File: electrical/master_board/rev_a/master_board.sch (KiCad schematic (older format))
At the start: 4 parts

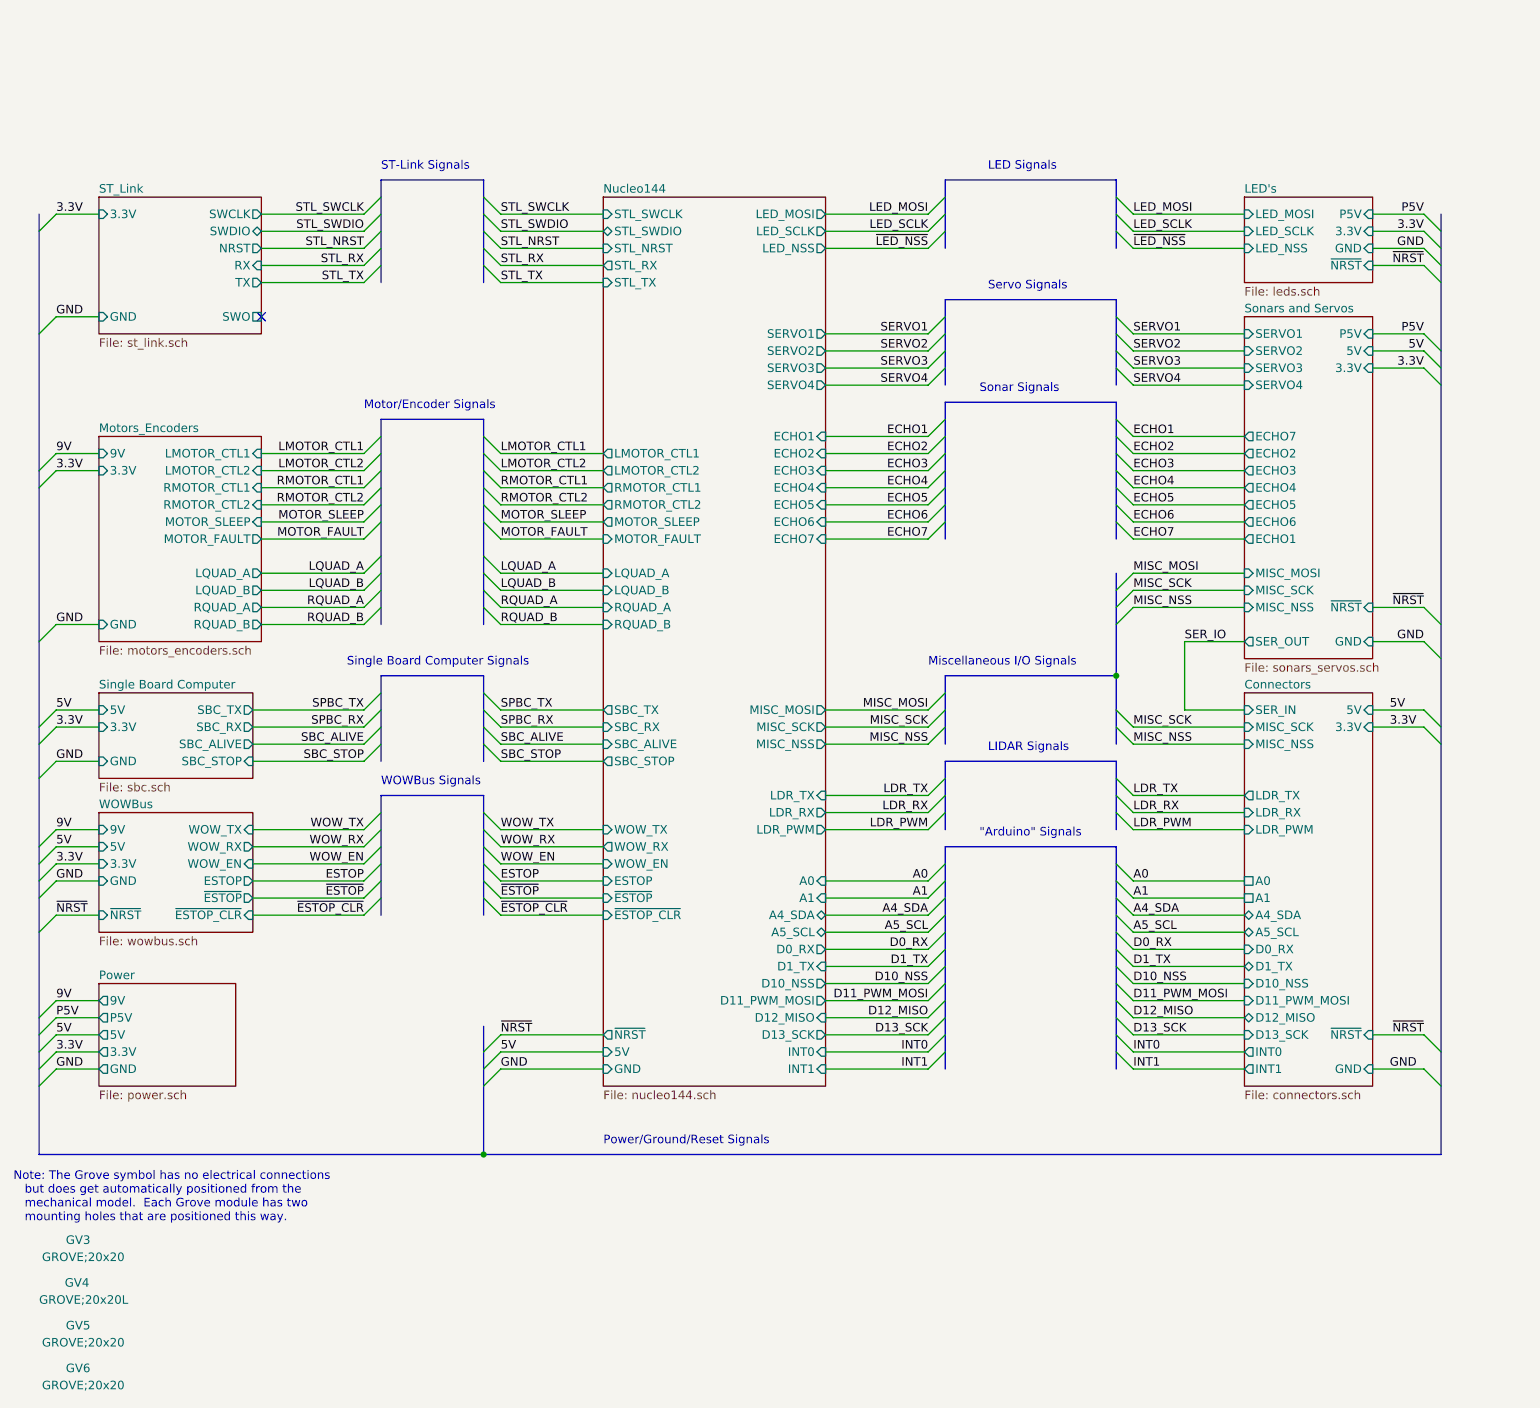
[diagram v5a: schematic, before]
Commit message: Bound signals to Morpho pins.
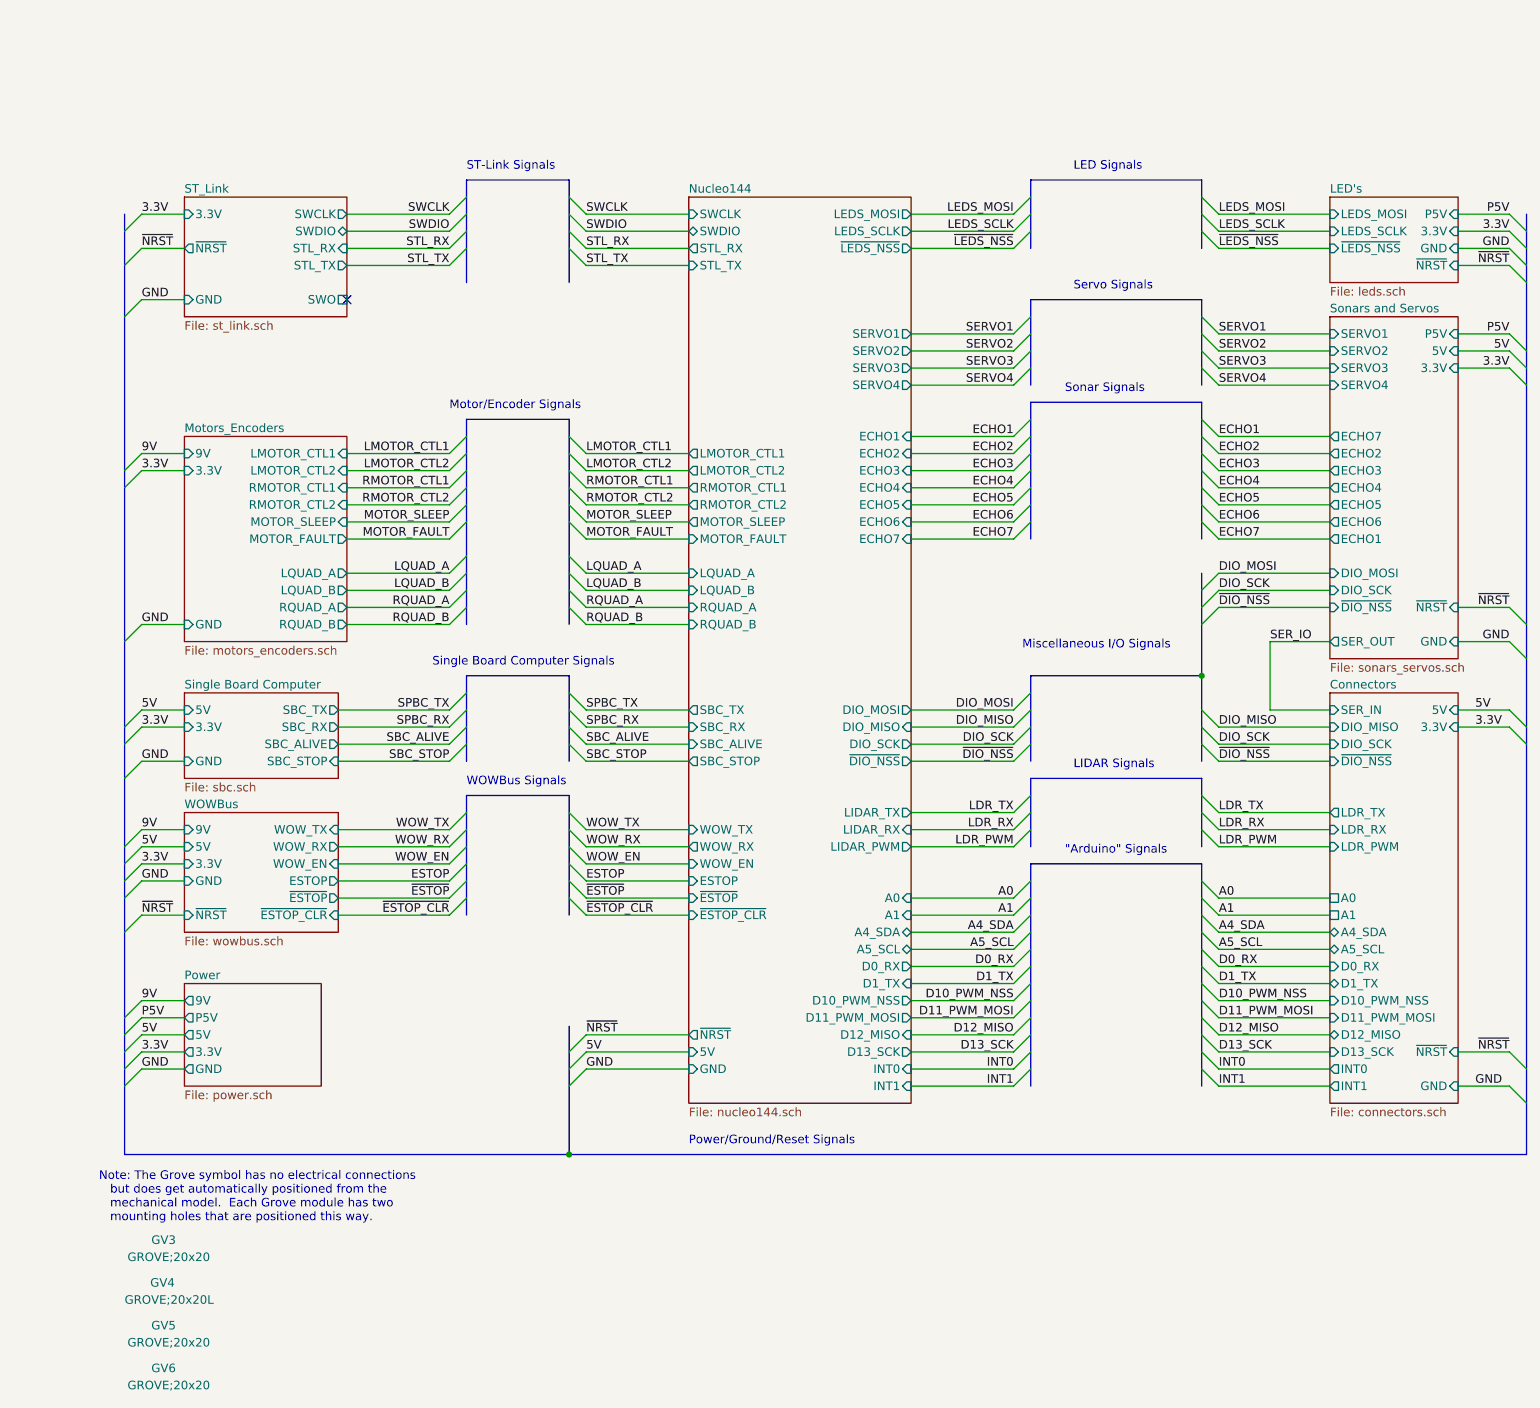
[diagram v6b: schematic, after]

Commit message: Schematic is basically complete.
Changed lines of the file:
@@
 RMOTOR_CTL1
 Text Label 4000 2800 0    50   ~ 0
-MOTOR_SLEEP
+~MOTOR_SLEEP
 Text Label 4000 2900 0    50   ~ 0
-MOTOR_FAULT
+~MOTOR_FAULT
 Text Label 4000 3100 0    50   ~ 0
 LQUAD_A
@@
 LQUAD_A
 Text Label 3200 2900 2    50   ~ 0
-MOTOR_FAULT
-Text Label 3200 2800 2    50   ~ 0
-MOTOR_SLEEP
+~MOTOR_FAULT
 Text Label 3200 2600 2    50   ~ 0
 RMOTOR_CTL1
@@
 Wire Bus Line
 	3900 2200 3300 2200
-$Sheet
-S 1650 2300 950  1200
-U 5F4A826A
-F0 "Motors_Encoders" 50
-F1 "motors_encoders.sch" 50
-F2 "LMOTOR_CTL2" I R 2600 2500 50
-F3 "RMOTOR_CTL2" I R 2600 2700 50
-F4 "RMOTOR_CTL1" I R 2600 2600 50
-F5 "9V" I L 1650 2400 50
-F6 "LMOTOR_CTL1" I R 2600 2400 50
-F7 "MOTOR_SLEEP" I R 2600 2800 50
-F8 "MOTOR_FAULT" O R 2600 2900 50
-F9 "3.3V" I L 1650 2500 50
-F10 "LQUAD_B" O R 2600 3200 50
-F11 "LQUAD_A" O R 2600 3100 50
-F12 "RQUAD_A" O R 2600 3300 50
-F13 "RQUAD_B" O R 2600 3400 50
-F14 "GND" I L 1650 3400 50
-$EndSheet
 Text Label 7700 5700 0    50   ~ 0
 D11_PWM_MOSI
@@
 ~NRST
 $Sheet
-S 1650 4500 900  700
+S 1650 4500 900  800
 U 5F8C2F57
 F0 "WOWBus" 50
@@
 F2 "9V" I L 1650 4600 50
 F3 "GND" I L 1650 4900 50
-F4 "WOW_EN" I R 2550 4800 50
-F5 "3.3V" I L 1650 4800 50
-F6 "5V" I L 1650 4700 50
-F7 "WOW_TX" I R 2550 4600 50
-F8 "WOW_RX" O R 2550 4700 50
-F9 "ESTOP" O R 2550 4900 50
-F10 "~ESTOP" O R 2550 5000 50
-F11 "~ESTOP_CLR" I R 2550 5100 50
-F12 "~NRST" I L 1650 5100 50
+F4 "3.3V" I L 1650 4800 50
+F5 "5V" I L 1650 4700 50
+F6 "WOW_TX" I R 2550 4600 50
+F7 "WOW_RX" O R 2550 4700 50
+F8 "~ESTOP_CLR" I R 2550 5100 50
+F9 "~NRST" I L 1650 5100 50
+F10 "~MOTOR_FAULT" I R 2550 5200 50
+F11 "ESTOP" O R 2550 4900 50
+F12 "~ESTOP" O R 2550 5000 50
+F13 "WOW_EN" I R 2550 4800 50
 $EndSheet
 Wire Wire Line
@@
 F6 "3.3V" I L 1650 4000 50
 F7 "SBC_ALIVE" O R 2550 4100 50
-F8 "SBC_STOP" I R 2550 4200 50
 $EndSheet
-Text Label 3200 4200 2    50   ~ 0
-SBC_STOP
 Wire Wire Line
 	2550 3900 3200 3900
@@
 Wire Wire Line
 	2550 4100 3200 4100
-Wire Wire Line
-	2550 4200 3200 4200
-Entry Wire Line
-	3300 4100 3200 4200
 Entry Wire Line
 	3300 4000 3200 4100
@@
 Entry Wire Line
 	3200 3900 3300 3800
-Entry Wire Line
-	3900 4100 4000 4200
 Entry Wire Line
 	3900 4000 4000 4100
@@
 Text Label 4000 4100 0    50   ~ 0
 SBC_ALIVE
-Text Label 4000 4200 0    50   ~ 0
-SBC_STOP
 Wire Wire Line
 	4000 3900 4600 3900
@@
 Wire Wire Line
 	4000 4100 4600 4100
-Wire Wire Line
-	4000 4200 4600 4200
 Wire Bus Line
 	3300 3700 3900 3700
@@
 Text Notes 6800 4750 0    50   ~ 0
 "Arduino" Signals
-$Sheet
-S 4600 900  1300 5300
-U 5F3221A2
-F0 "Nucleo144" 50
-F1 "nucleo144.sch" 50
-F2 "GND" I L 4600 6000 50
-F3 "5V" I L 4600 5900 50
-F4 "STL_RX" O L 4600 1200 50
-F5 "STL_TX" I L 4600 1300 50
-F6 "LMOTOR_CTL1" O L 4600 2400 50
-F7 "LMOTOR_CTL2" O L 4600 2500 50
-F8 "RMOTOR_CTL1" O L 4600 2600 50
-F9 "RMOTOR_CTL2" O L 4600 2700 50
-F10 "MOTOR_SLEEP" O L 4600 2800 50
-F11 "MOTOR_FAULT" I L 4600 2900 50
-F12 "LQUAD_A" I L 4600 3100 50
-F13 "LQUAD_B" I L 4600 3200 50
-F14 "RQUAD_A" I L 4600 3300 50
-F15 "RQUAD_B" I L 4600 3400 50
-F16 "ECHO1" I R 5900 2300 50
-F17 "ECHO2" I R 5900 2400 50
-F18 "ECHO3" I R 5900 2500 50
-F19 "ECHO4" I R 5900 2600 50
-F20 "ECHO5" I R 5900 2700 50
-F21 "ECHO6" I R 5900 2800 50
-F22 "ECHO7" I R 5900 2900 50
-F23 "SERVO2" O R 5900 1800 50
-F24 "SERVO1" O R 5900 1700 50
-F25 "SERVO3" O R 5900 1900 50
-F26 "SERVO4" O R 5900 2000 50
-F27 "A0" I R 5900 5000 50
-F28 "A1" I R 5900 5100 50
-F29 "A4_SDA" B R 5900 5200 50
-F30 "A5_SCL" B R 5900 5300 50
-F31 "D0_RX" O R 5900 5400 50
-F32 "D1_TX" I R 5900 5500 50
-F33 "D11_PWM_MOSI" O R 5900 5700 50
-F34 "D12_MISO" I R 5900 5800 50
-F35 "D13_SCK" O R 5900 5900 50
-F36 "~NRST" O L 4600 5800 50
-F37 "INT0" I R 5900 6000 50
-F38 "INT1" I R 5900 6100 50
-F39 "WOW_TX" I L 4600 4600 50
-F40 "WOW_RX" O L 4600 4700 50
-F41 "WOW_EN" I L 4600 4800 50
-F42 "ESTOP" I L 4600 4900 50
-F43 "~ESTOP" I L 4600 5000 50
-F44 "~ESTOP_CLR" I L 4600 5100 50
-F45 "SBC_TX" O L 4600 3900 50
-F46 "SBC_RX" I L 4600 4000 50
-F47 "SBC_ALIVE" I L 4600 4100 50
-F48 "SBC_STOP" O L 4600 4200 50
-F49 "LEDS_MOSI" O R 5900 1000 50
-F50 "LEDS_SCLK" O R 5900 1100 50
-F51 "SWCLK" I L 4600 1000 50
-F52 "SWDIO" B L 4600 1100 50
-F53 "D10_PWM_NSS" O R 5900 5600 50
-F54 "LIDAR_PWM" O R 5900 4700 50
-F55 "LIDAR_TX" O R 5900 4500 50
-F56 "LIDAR_RX" I R 5900 4600 50
-F57 "DIO_MOSI" O R 5900 3900 50
-F58 "DIO_SCK" O R 5900 4100 50
-F59 "DIO_MISO" I R 5900 4000 50
-F60 "~DIO_NSS" O R 5900 4200 50
-F61 "~LEDS_NSS" O R 5900 1200 50
-$EndSheet
 Entry Wire Line
 	6500 3900 6600 3800
@@
 Text Label 1400 1200 0    50   ~ 0
 ~NRST
+$Sheet
+S 1650 2300 950  1200
+U 5F4A826A
+F0 "Motors_Encoders" 50
+F1 "motors_encoders.sch" 50
+F2 "LMOTOR_CTL2" I R 2600 2500 50
+F3 "RMOTOR_CTL2" I R 2600 2700 50
+F4 "RMOTOR_CTL1" I R 2600 2600 50
+F5 "9V" I L 1650 2400 50
+F6 "LMOTOR_CTL1" I R 2600 2400 50
+F7 "3.3V" I L 1650 2500 50
+F8 "LQUAD_B" O R 2600 3200 50
+F9 "LQUAD_A" O R 2600 3100 50
+F10 "RQUAD_A" O R 2600 3300 50
+F11 "RQUAD_B" O R 2600 3400 50
+F12 "GND" I L 1650 3400 50
+F13 "~MOTOR_SLEEP" I R 2600 2800 50
+F14 "~MOTOR_FAULT" O R 2600 2900 50
+$EndSheet
+Text Label 3200 2800 2    50   ~ 0
+~MOTOR_SLEEP
+Entry Wire Line
+	3200 5200 3300 5100
+Entry Wire Line
+	4000 5200 3900 5100
+Wire Wire Line
+	2550 5200 3200 5200
+Wire Wire Line
+	4600 5200 4000 5200
+Text Label 3200 5200 2    50   ~ 0
+~MOTOR_FAULT
+Text Label 4000 5200 0    50   ~ 0
+~MOTOR_FAULT
+$Sheet
+S 4600 900  1300 5300
+U 5F3221A2
+F0 "Nucleo144" 50
+F1 "nucleo144.sch" 50
+F2 "GND" I L 4600 6000 50
+F3 "5V" I L 4600 5900 50
+F4 "STL_RX" O L 4600 1200 50
+F5 "STL_TX" I L 4600 1300 50
+F6 "LMOTOR_CTL1" O L 4600 2400 50
+F7 "LMOTOR_CTL2" O L 4600 2500 50
+F8 "RMOTOR_CTL1" O L 4600 2600 50
+F9 "RMOTOR_CTL2" O L 4600 2700 50
+F10 "LQUAD_A" I L 4600 3100 50
+F11 "LQUAD_B" I L 4600 3200 50
+F12 "RQUAD_A" I L 4600 3300 50
+F13 "RQUAD_B" I L 4600 3400 50
+F14 "ECHO1" I R 5900 2300 50
+F15 "ECHO2" I R 5900 2400 50
+F16 "ECHO3" I R 5900 2500 50
+F17 "ECHO4" I R 5900 2600 50
+F18 "ECHO5" I R 5900 2700 50
+F19 "ECHO6" I R 5900 2800 50
+F20 "ECHO7" I R 5900 2900 50
+F21 "SERVO2" O R 5900 1800 50
+F22 "SERVO1" O R 5900 1700 50
+F23 "SERVO3" O R 5900 1900 50
+F24 "SERVO4" O R 5900 2000 50
+F25 "A0" I R 5900 5000 50
+F26 "A1" I R 5900 5100 50
+F27 "A4_SDA" B R 5900 5200 50
+F28 "A5_SCL" B R 5900 5300 50
+F29 "D0_RX" O R 5900 5400 50
+F30 "D1_TX" I R 5900 5500 50
+F31 "D11_PWM_MOSI" O R 5900 5700 50
+F32 "D12_MISO" I R 5900 5800 50
+F33 "D13_SCK" O R 5900 5900 50
+F34 "~NRST" O L 4600 5800 50
+F35 "INT0" I R 5900 6000 50
+F36 "INT1" I R 5900 6100 50
+F37 "WOW_TX" I L 4600 4600 50
+F38 "WOW_RX" O L 4600 4700 50
+F39 "~ESTOP_CLR" I L 4600 5100 50
+F40 "SBC_TX" O L 4600 3900 50
+F41 "SBC_RX" I L 4600 4000 50
+F42 "SBC_ALIVE" I L 4600 4100 50
+F43 "LEDS_MOSI" O R 5900 1000 50
+F44 "LEDS_SCLK" O R 5900 1100 50
+F45 "SWCLK" I L 4600 1000 50
+F46 "SWDIO" B L 4600 1100 50
+F47 "D10_PWM_NSS" O R 5900 5600 50
+F48 "LIDAR_PWM" O R 5900 4700 50
+F49 "LIDAR_TX" O R 5900 4500 50
+F50 "LIDAR_RX" I R 5900 4600 50
+F51 "DIO_MOSI" O R 5900 3900 50
+F52 "DIO_SCK" O R 5900 4100 50
+F53 "DIO_MISO" I R 5900 4000 50
+F54 "~DIO_NSS" O R 5900 4200 50
+F55 "~LEDS_NSS" O R 5900 1200 50
+F56 "~MOTOR_FAULT_IN" I L 4600 2900 50
+F57 "~MOTOR_FAULT_OUT" O L 4600 5200 50
+F58 "~MOTOR_SLEEP" O L 4600 2800 50
+F59 "ESTOP" I L 4600 4900 50
+F60 "~ESTOP_IN" I L 4600 5000 50
+F61 "WOW_EN" O L 4600 4800 50
+$EndSheet
 Wire Bus Line
 	7600 3700 7600 4200
@@
 	3900 800  3900 1400
 Wire Bus Line
+	3300 3700 3300 4100
+Wire Bus Line
+	3900 3700 3900 4100
+Wire Bus Line
 	6600 1500 6600 2000
 Wire Bus Line
 	6600 3700 6600 4200
 Wire Bus Line
-	3300 4400 3300 5100
-Wire Bus Line
-	3900 4400 3900 5100
-Wire Bus Line
-	3300 3700 3300 4200
-Wire Bus Line
-	3900 3700 3900 4200
+	3300 4400 3300 5200
+Wire Bus Line
+	3900 4400 3900 5200
 Wire Bus Line
 	3300 2200 3300 3400
